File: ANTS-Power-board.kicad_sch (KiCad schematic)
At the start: 0 parts

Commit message: add connections
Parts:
- added MH1, MH2, MH3, MH4: M3, MountingHole:MountingHole_3.2mm_M3_Pad_Via, symbol Mechanical:MountingHole_Pad
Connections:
- new net GND: MH1.1, MH2.1, MH3.1, MH4.1
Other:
- note added: "5V OUTPUT TERMINAL BLOCKS"
- note added: "BATTERY PACK 1 CONNECTION"

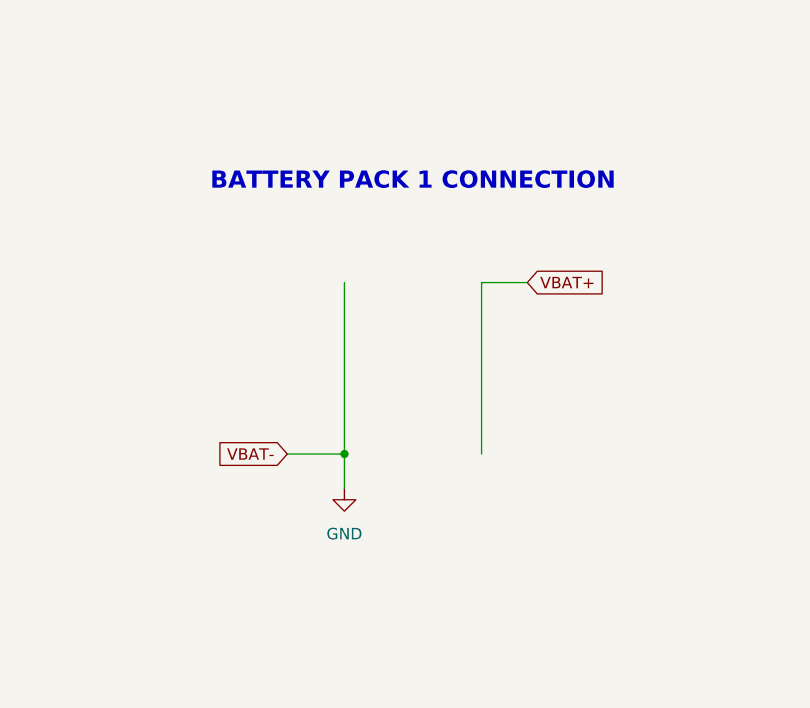
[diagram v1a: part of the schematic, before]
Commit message: Import one DF11
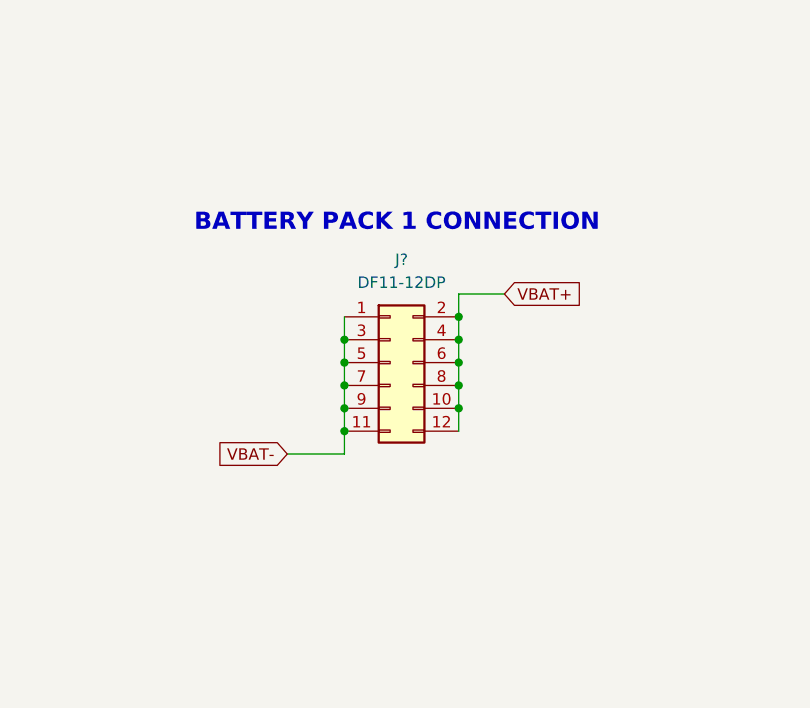
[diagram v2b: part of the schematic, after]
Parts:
- added J?: DF11-12DP, Connector_Hirose:Hirose_DF11-12DP-2DSA_2x06_P2.00mm_Vertical, symbol Connector_Generic:Conn_02x06_Odd_Even
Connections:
- net VBAT+: now also J?.10 (Pin_10), J?.12 (Pin_12), J?.2 (Pin_2), J?.4 (Pin_4), J?.6 (Pin_6), J?.8 (Pin_8)
- new net VBAT-: J?.1 (Pin_1), J?.11 (Pin_11), J?.3 (Pin_3), J?.5 (Pin_5), J?.7 (Pin_7), J?.9 (Pin_9)
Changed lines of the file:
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@@
 	(text "BATTERY PACK 1 CONNECTION"
 		(exclude_from_sim no)
-		(at 121.92 42.164 0)
+		(at 120.142 46.736 0)
 		(effects
 			(font
@@
 	)
 	(junction
-		(at 114.3 72.39)
+		(at 114.3 67.31)
+		(diameter 0)
+		(color 0 0 0 0)
+	)
+	(junction
+		(at 127 59.69)
+		(diameter 0)
+		(color 0 0 0 0)
+	)
+	(junction
+		(at 127 67.31)
+		(diameter 0)
+		(color 0 0 0 0)
+	)
+	(junction
+		(at 127 57.15)
+		(diameter 0)
+		(color 0 0 0 0)
+	)
+	(junction
+		(at 114.3 69.85)
+		(diameter 0)
+		(color 0 0 0 0)
+	)
+	(junction
+		(at 127 62.23)
+		(diameter 0)
+		(color 0 0 0 0)
+	)
+	(junction
+		(at 114.3 62.23)
 		(diameter 0)
 		(color 0 0 0 0)
@@
 	)
 	(junction
+		(at 114.3 64.77)
+		(diameter 0)
+		(color 0 0 0 0)
+	)
+	(junction
+		(at 114.3 59.69)
+		(diameter 0)
+		(color 0 0 0 0)
+	)
+	(junction
 		(at 38.1 181.61)
 		(diameter 0)
 		(color 0 0 0 0)
 	)
+	(junction
+		(at 127 64.77)
+		(diameter 0)
+		(color 0 0 0 0)
+	)
+	(wire
+		(pts
+			(xy 114.3 59.69) (xy 114.3 62.23)
+		)
+		(stroke
+			(width 0)
+			(type default)
+		)
+	)
+	(wire
+		(pts
+			(xy 127 59.69) (xy 127 62.23)
+		)
+		(stroke
+			(width 0)
+			(type default)
+		)
+	)
 	(wire
 		(pts
@@
 	(wire
 		(pts
-			(xy 114.3 53.34) (xy 114.3 72.39)
-		)
-		(stroke
-			(width 0)
-			(type default)
-		)
-	)
-	(wire
-		(pts
-			(xy 114.3 72.39) (xy 114.3 76.2)
-		)
-		(stroke
-			(width 0)
-			(type default)
-		)
-	)
-	(wire
-		(pts
-			(xy 129.54 53.34) (xy 129.54 72.39)
+			(xy 127 62.23) (xy 127 64.77)
+		)
+		(stroke
+			(width 0)
+			(type default)
+		)
+	)
+	(wire
+		(pts
+			(xy 114.3 69.85) (xy 114.3 72.39)
+		)
+		(stroke
+			(width 0)
+			(type default)
+		)
+	)
+	(wire
+		(pts
+			(xy 114.3 62.23) (xy 114.3 64.77)
+		)
+		(stroke
+			(width 0)
+			(type default)
+		)
+	)
+	(wire
+		(pts
+			(xy 127 57.15) (xy 127 59.69)
+		)
+		(stroke
+			(width 0)
+			(type default)
+		)
+	)
+	(wire
+		(pts
+			(xy 127 54.61) (xy 127 57.15)
+		)
+		(stroke
+			(width 0)
+			(type default)
+		)
+	)
+	(wire
+		(pts
+			(xy 114.3 57.15) (xy 114.3 59.69)
+		)
+		(stroke
+			(width 0)
+			(type default)
+		)
+	)
+	(wire
+		(pts
+			(xy 114.3 67.31) (xy 114.3 69.85)
 		)
 		(stroke
@@
 	(wire
 		(pts
+			(xy 127 67.31) (xy 127 69.85)
+		)
+		(stroke
+			(width 0)
+			(type default)
+		)
+	)
+	(wire
+		(pts
 			(xy 58.42 181.61) (xy 48.26 181.61)
 		)
@@
 	(wire
 		(pts
+			(xy 127 64.77) (xy 127 67.31)
+		)
+		(stroke
+			(width 0)
+			(type default)
+		)
+	)
+	(wire
+		(pts
+			(xy 114.3 64.77) (xy 114.3 67.31)
+		)
+		(stroke
+			(width 0)
+			(type default)
+		)
+	)
+	(wire
+		(pts
 			(xy 107.95 72.39) (xy 114.3 72.39)
 		)
@@
 	(wire
 		(pts
-			(xy 134.62 53.34) (xy 129.54 53.34)
+			(xy 132.08 54.61) (xy 127 54.61)
 		)
 		(stroke
@@
 	(global_label "VBAT+"
 		(shape input)
-		(at 134.62 53.34 0)
+		(at 132.08 54.61 0)
 		(fields_autoplaced yes)
 		(effects
@@
 		)
 		(property "Intersheetrefs" "${INTERSHEET_REFS}"
-			(at 143.5924 53.34 0)
+			(at 141.0524 54.61 0)
 			(effects
 				(font
@@
 	)
 	(symbol
-		(lib_id "power:GND")
-		(at 114.3 76.2 0)
-		(mirror y)
+		(lib_id "Connector_Generic:Conn_02x06_Odd_Even")
+		(at 119.38 62.23 0)
 		(unit 1)
 		(exclude_from_sim no)
@@
 		(dnp no)
 		(fields_autoplaced yes)
-		(property "Reference" "#PWR09"
-			(at 114.3 82.55 0)
-			(effects
-				(font
-					(size 1.27 1.27)
-				)
-				(hide yes)
-			)
-		)
-		(property "Value" "GND"
-			(at 114.3 81.28 0)
-			(effects
-				(font
-					(size 1.27 1.27)
-				)
-			)
-		)
-		(property "Footprint" ""
-			(at 114.3 76.2 0)
-			(effects
-				(font
-					(size 1.27 1.27)
-				)
-				(hide yes)
-			)
-		)
-		(property "Datasheet" ""
-			(at 114.3 76.2 0)
-			(effects
-				(font
-					(size 1.27 1.27)
-				)
-				(hide yes)
-			)
-		)
-		(property "Description" "Power symbol creates a global label with name \"GND\" , ground"
-			(at 114.3 76.2 0)
-			(effects
-				(font
-					(size 1.27 1.27)
-				)
-				(hide yes)
-			)
+		(property "Reference" "J?"
+			(at 120.65 50.8 0)
+			(effects
+				(font
+					(size 1.27 1.27)
+				)
+			)
+		)
+		(property "Value" "DF11-12DP"
+			(at 120.65 53.34 0)
+			(effects
+				(font
+					(size 1.27 1.27)
+				)
+			)
+		)
+		(property "Footprint" "Connector_Hirose:Hirose_DF11-12DP-2DSA_2x06_P2.00mm_Vertical"
+			(at 119.38 62.23 0)
+			(effects
+				(font
+					(size 1.27 1.27)
+				)
+				(hide yes)
+			)
+		)
+		(property "Datasheet" "~"
+			(at 119.38 62.23 0)
+			(effects
+				(font
+					(size 1.27 1.27)
+				)
+				(hide yes)
+			)
+		)
+		(property "Description" "Generic connector, double row, 02x06, odd/even pin numbering scheme (row 1 odd numbers, row 2 even numbers), script generated (kicad-library-utils/schlib/autogen/connector/)"
+			(at 119.38 62.23 0)
+			(effects
+				(font
+					(size 1.27 1.27)
+				)
+				(hide yes)
+			)
+		)
+		(pin "5"
+		)
+		(pin "9"
 		)
 		(pin "1"
 		)
+		(pin "3"
+		)
+		(pin "7"
+		)
+		(pin "11"
+		)
+		(pin "2"
+		)
+		(pin "4"
+		)
+		(pin "6"
+		)
+		(pin "8"
+		)
+		(pin "10"
+		)
+		(pin "12"
+		)
 		(instances
-			(project "ANTS-Power-board"
+			(project ""
 				(path "/4d632659-7d2f-4407-ada5-b4e72f7be845"
-					(reference "#PWR09")
+					(reference "J?")
 					(unit 1)
 				)
